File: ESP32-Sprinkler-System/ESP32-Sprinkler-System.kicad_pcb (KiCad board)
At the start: 2 copper layers, 135 x 87 mm, 62 parts, among them J101 12V, J102 DHT, J103 NEOPIXEL, J104 LCD, J105 BME280, J201 TBL004-508-02BE-2GY, J202 TBL004-508-02BE-2GY, J203 TBL004-508-02BE-2GY, J204 TBL004-508-02BE-2GY, Q201 IRFZ24NPBF, Q202 IRFZ24NPBF, Q203 IRFZ24NPBF, Q204 IRFZ24NPBF, U101 V7805-500, U102 ESP32-DEVKITC-32D, U201 MC33152PG, U202 MC33152PG

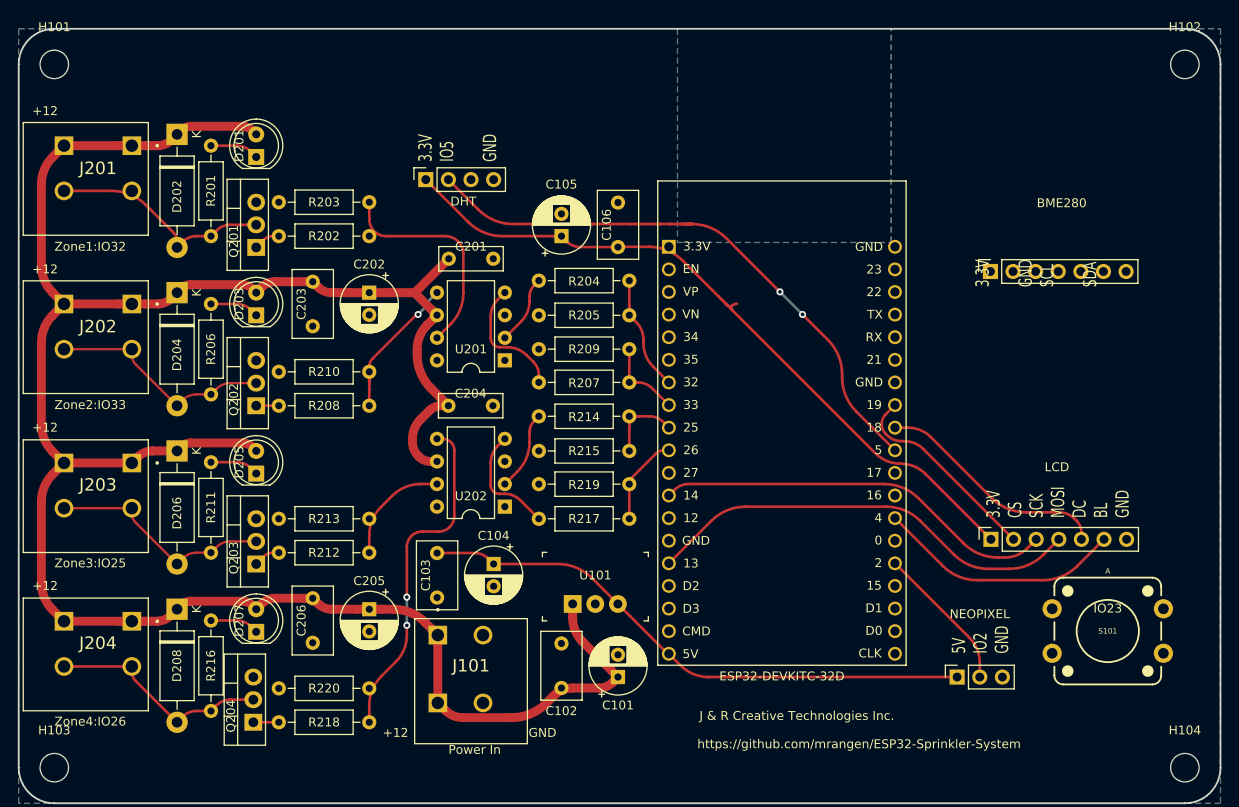
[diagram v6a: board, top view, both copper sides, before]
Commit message: Tidy up
moved labels and reconnected traces
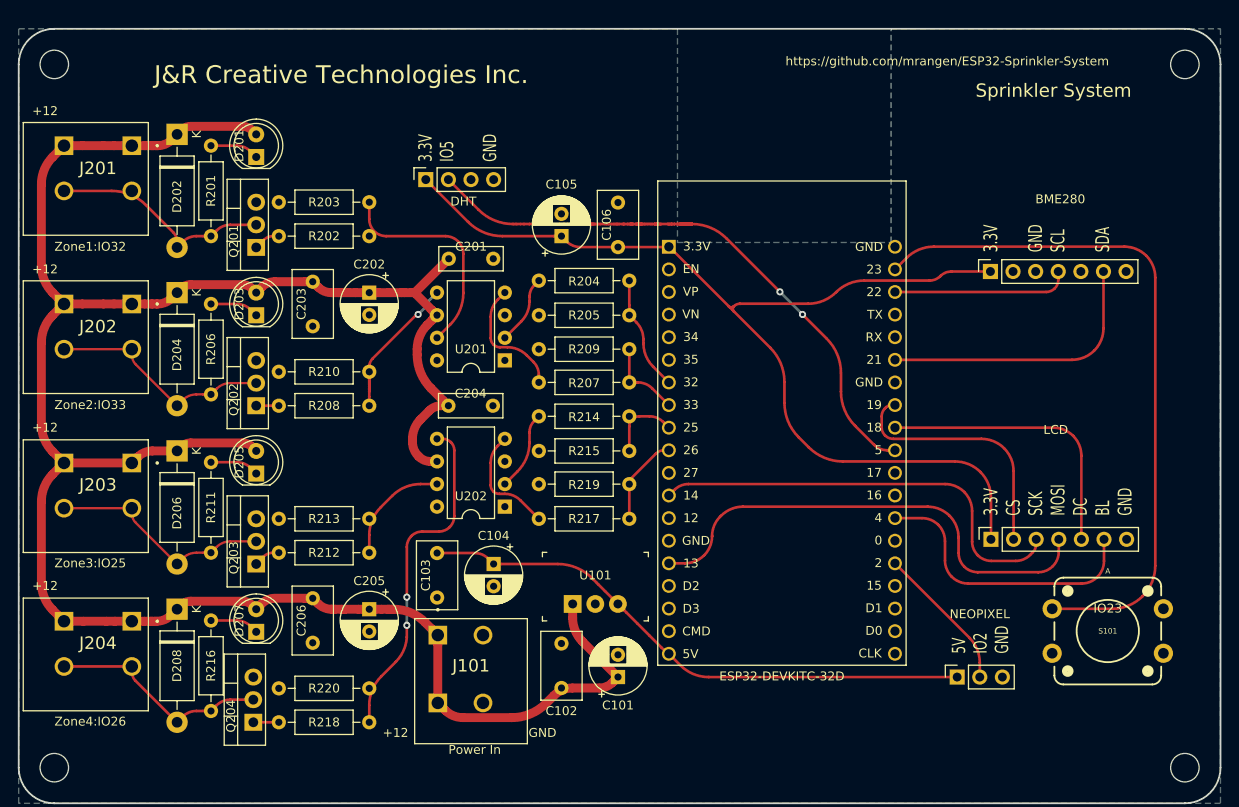
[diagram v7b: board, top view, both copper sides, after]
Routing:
- net SW_A: track 0.00 -> 78.7 mm
- net 3.3V: track 80.8 -> 117.5 mm
- net SDA: track 0.00 -> 31.8 mm
- net SCL: track 0.00 -> 20.0 mm
- net CS: track 22.9 -> 28.7 mm
- net D/C: track 26.4 -> 32.1 mm
- net MOSI: track 49.7 -> 54.9 mm
- net BACKLIGHT: track 27.7 -> 32.4 mm
- net SCK: track 45.3 -> 49.5 mm
- net DHT: track 64.6 -> 65.5 mm
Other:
- board text added: "J&R Creative Technologies Inc."
- board text added: "Sprinkler System"
- board text removed: "J & R Creative Technologies Inc."
